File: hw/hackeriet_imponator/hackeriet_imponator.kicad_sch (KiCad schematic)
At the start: 19 parts, among them J1 USB4085-GF-A, J2 UPDI Programming, J3 External Battery Connector, J4 Shitty Add On, J5 Unused pins, SW1 SW_SPDT, U1 ATtiny804-SS, U2 MCP2221AxSL

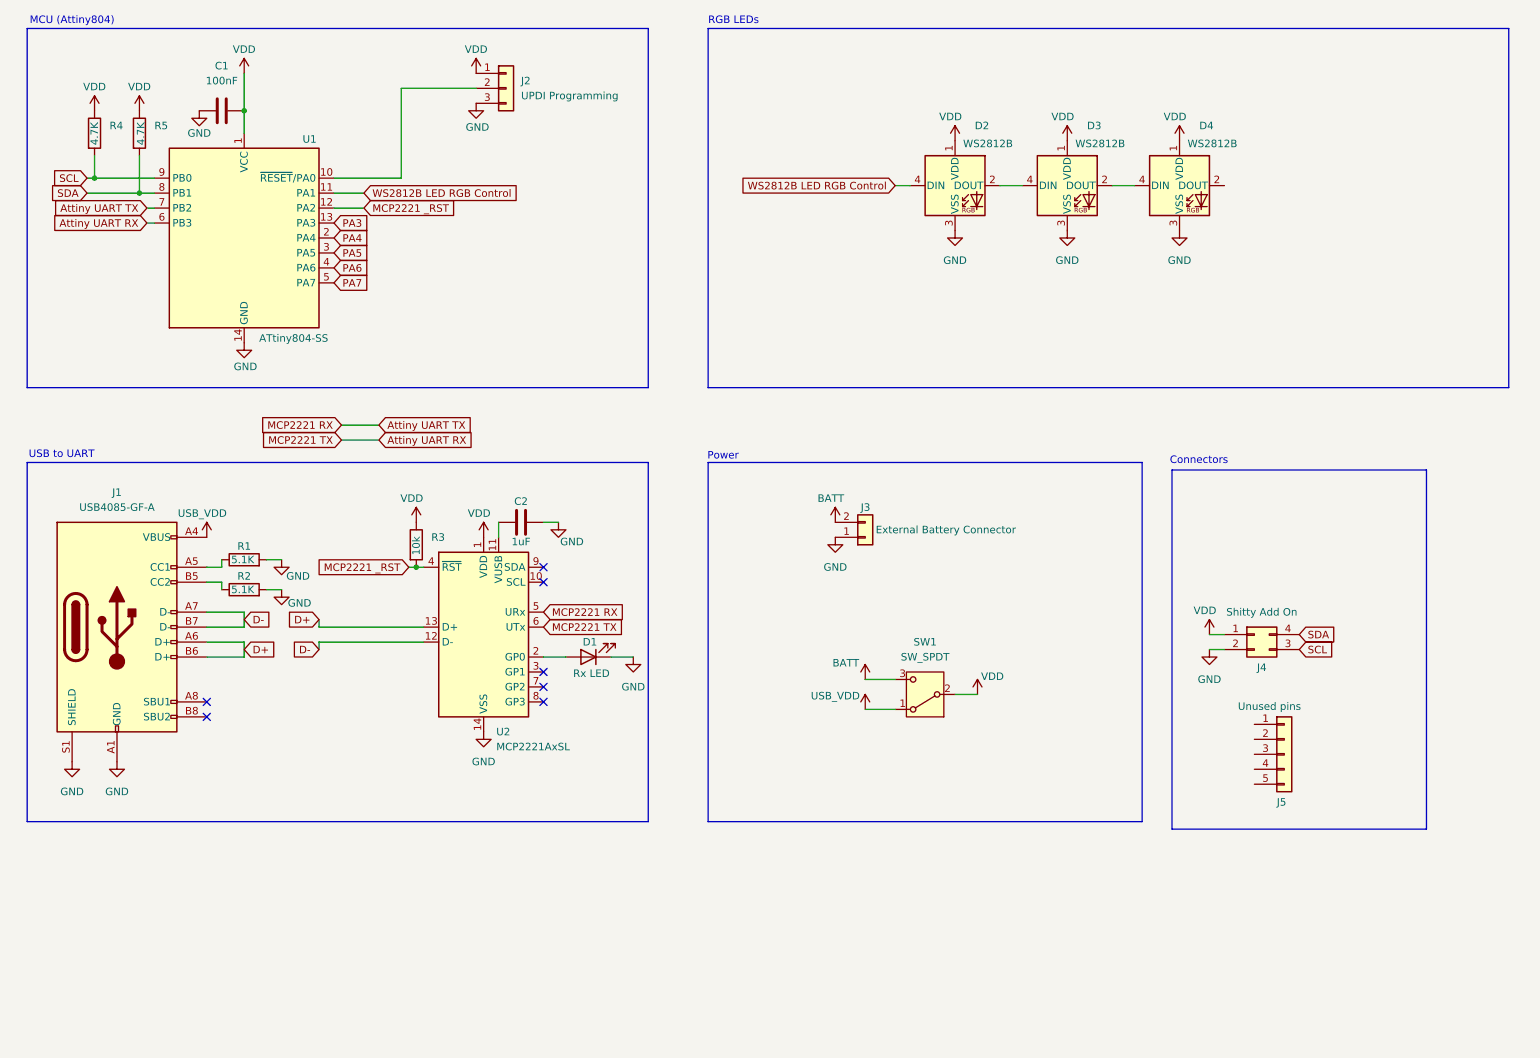
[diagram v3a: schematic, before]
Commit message: Fine-tuned silkscreen logo and LED spacing.
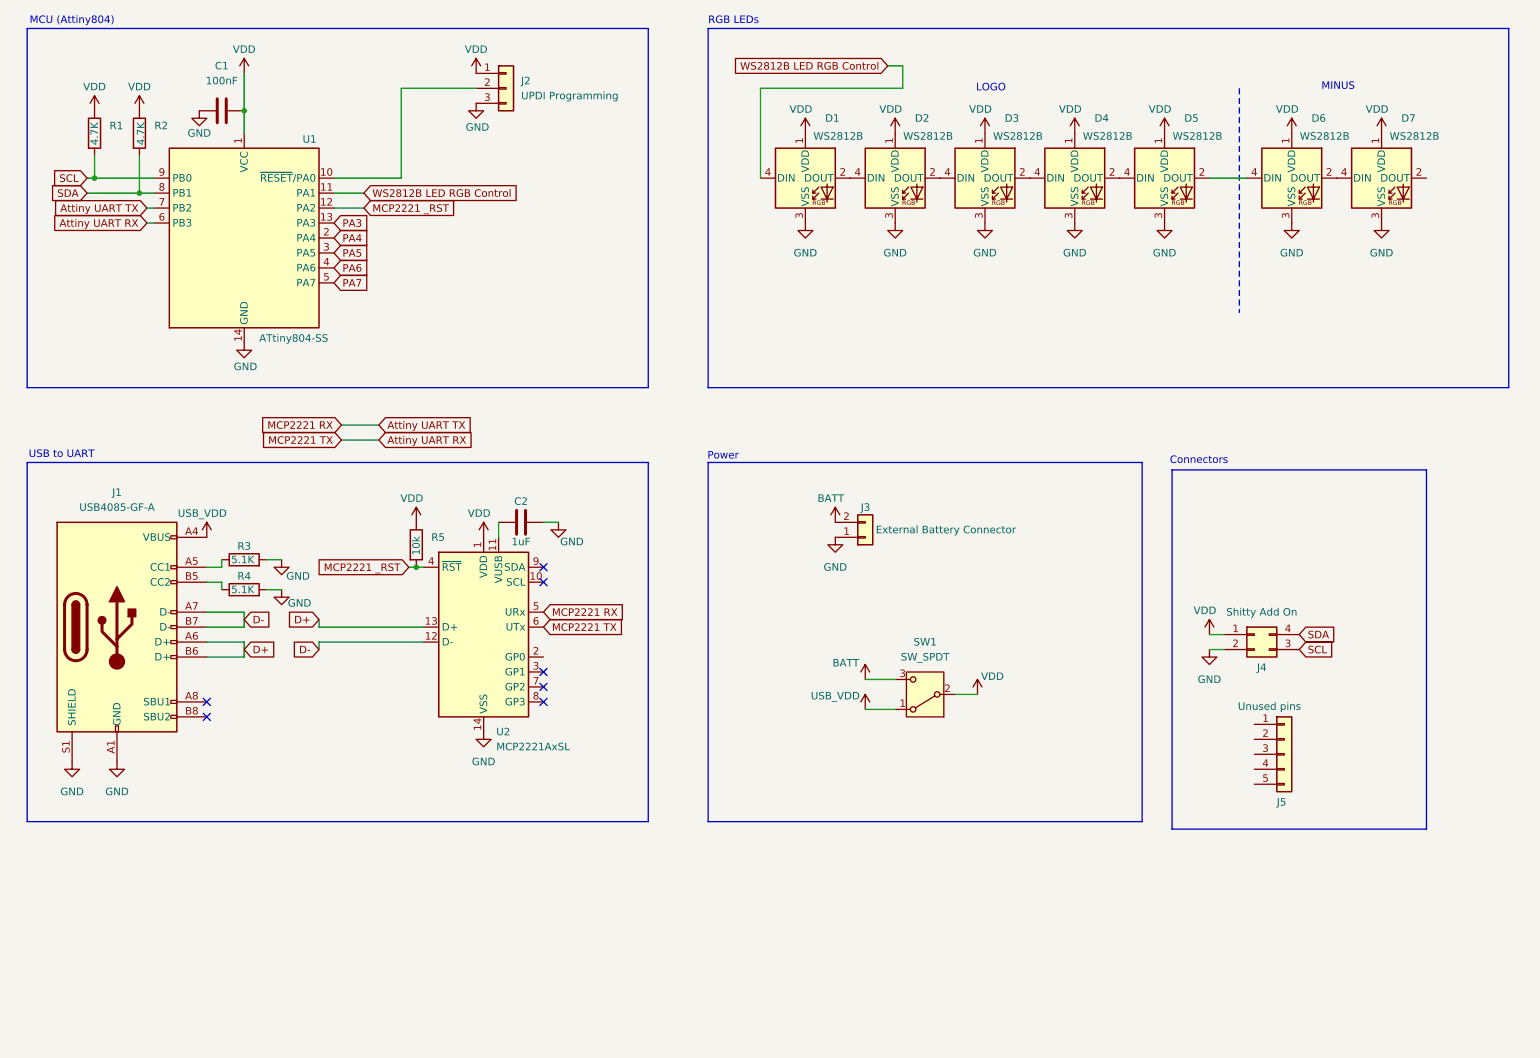
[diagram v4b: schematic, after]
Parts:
- removed D1: Rx LED, LED_SMD:LED_0603_1608Metric_Pad1.05x0.95mm_HandSolder, symbol Device:LED
- added D4, D5, D6, D7: WS2812B, imponator_footprint_lib:LED_WS2812B-4020, symbol LED:WS2812B
- renumbered D2 to D1, D4 to D2, R4 to R1, R5 to R2, R1 to R3, R2 to R4, R3 to R5
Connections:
- net GND: now also D4.3 (VSS), D5.3 (VSS), D6.3 (VSS), D7.3 (VSS)
- net VDD: now also D4.1 (VDD), D5.1 (VDD), D6.1 (VDD), D7.1 (VDD)
- net at D1.2 (DOUT): now also D2.4 (DIN); no longer D3.4 (DIN)
- net at D2.2 (DOUT): now also D3.4 (DIN)
- net at D3.2 (DOUT): now also D4.4 (DIN); no longer D2.4 (DIN)
- new net: D6.2 (DOUT), D7.4 (DIN)
- new net: D5.2 (DOUT), D6.4 (DIN)
- new net: D4.2 (DOUT), D5.4 (DIN)
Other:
- note added: "LOGO"
- note added: "MINUS"
- moved on the sheet: D1, D2

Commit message: Added accelerometer to schematic. Also crossed off some TODOs that were already done.
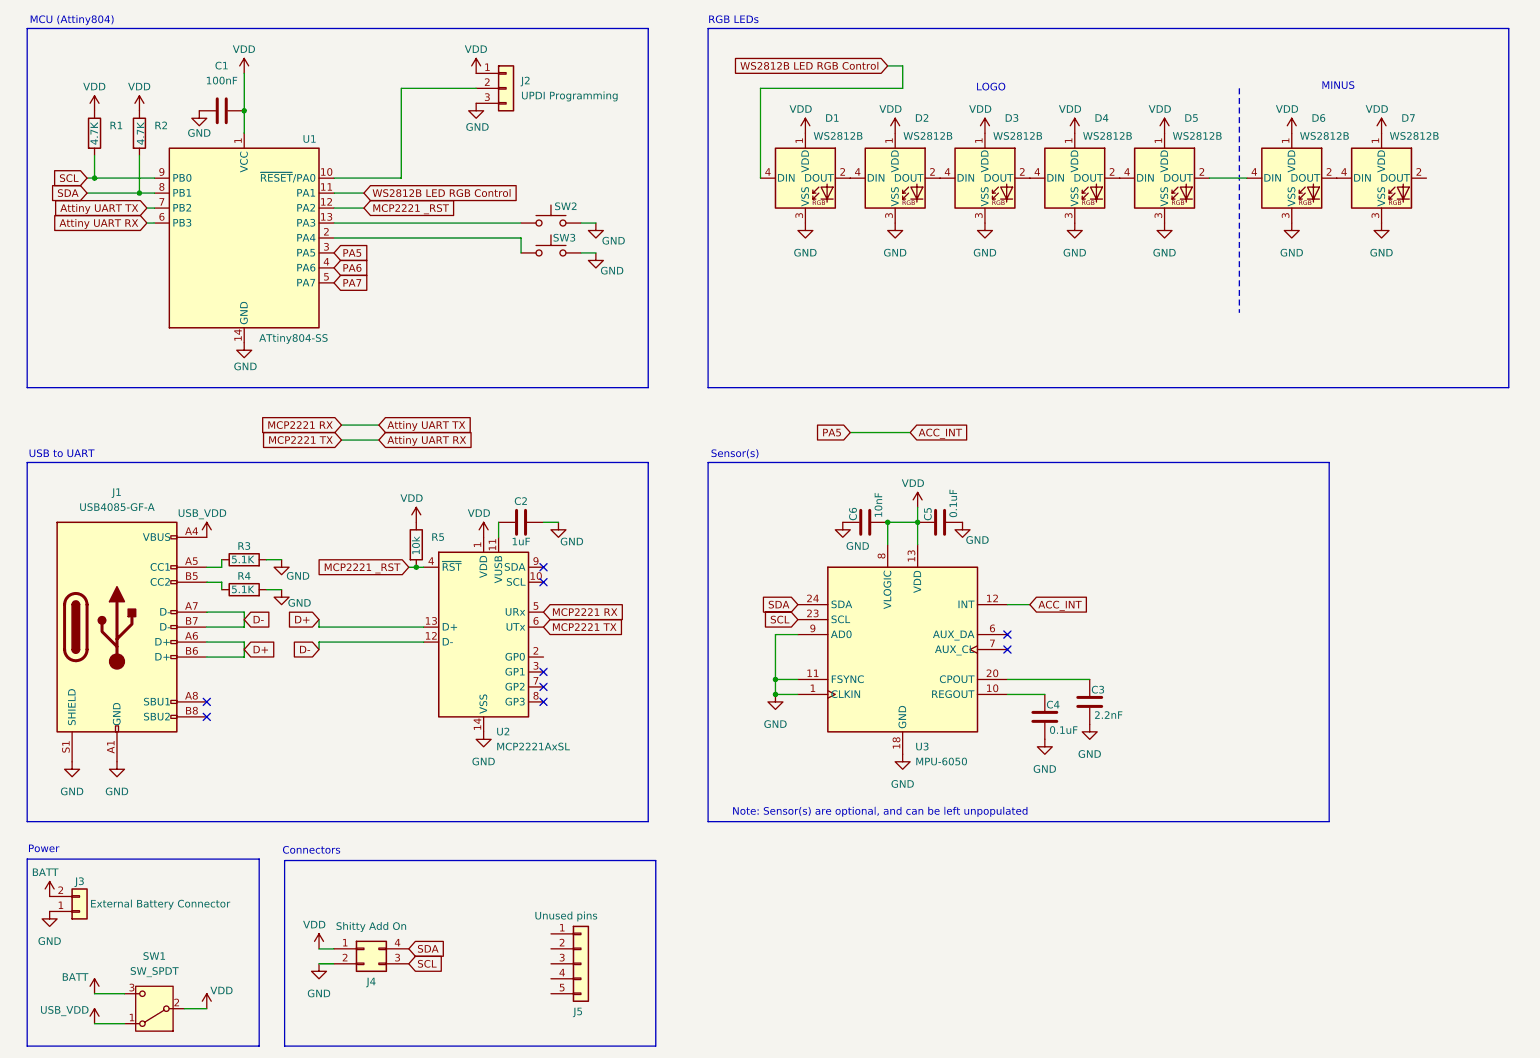
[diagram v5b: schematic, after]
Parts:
- added C3: 2.2nF, symbol Device:C
- added C4, C5: 0.1uF, symbol Device:C
- added C6: 10nF, symbol Device:C
- added SW2, SW3: User configurable, symbol Switch:SW_Push
- added U3: MPU-6050, Sensor_Motion:InvenSense_QFN-24_4x4mm_P0.5mm, symbol Sensor_Motion:MPU-6050
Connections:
- net GND: now also C3.1, C4.1, C5.1, C6.2, SW2.2, SW3.2, U3.1 (CLKIN), U3.11 (FSYNC), U3.18 (GND), U3.9 (AD0)
- net SCL: now also U3.23 (SCL)
- net SDA: now also U3.24 (SDA)
- net VDD: now also C5.2, C6.1, U3.13 (VDD), U3.8 (VLOGIC)
- net PA3: no longer names the net of U1.13 (PA3)
- net PA3: now also SW2.1
- net PA4: no longer names the net of U1.2 (PA4)
- net PA4: now also SW3.1
- net PA5 renamed ACC_INT
- net ACC_INT: now also U3.12 (INT)
- new net: C4.2, U3.10 (REGOUT)
- new net: C3.2, U3.20 (CPOUT)
- no-connect marks 7 -> 9
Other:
- note added: "Note: Sensor(s) are optional, and can be left unpopulated"
- note added: "Sensor(s)"
- moved on the sheet: J3, J4, J5, SW1

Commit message: Added LDO for accelerometer
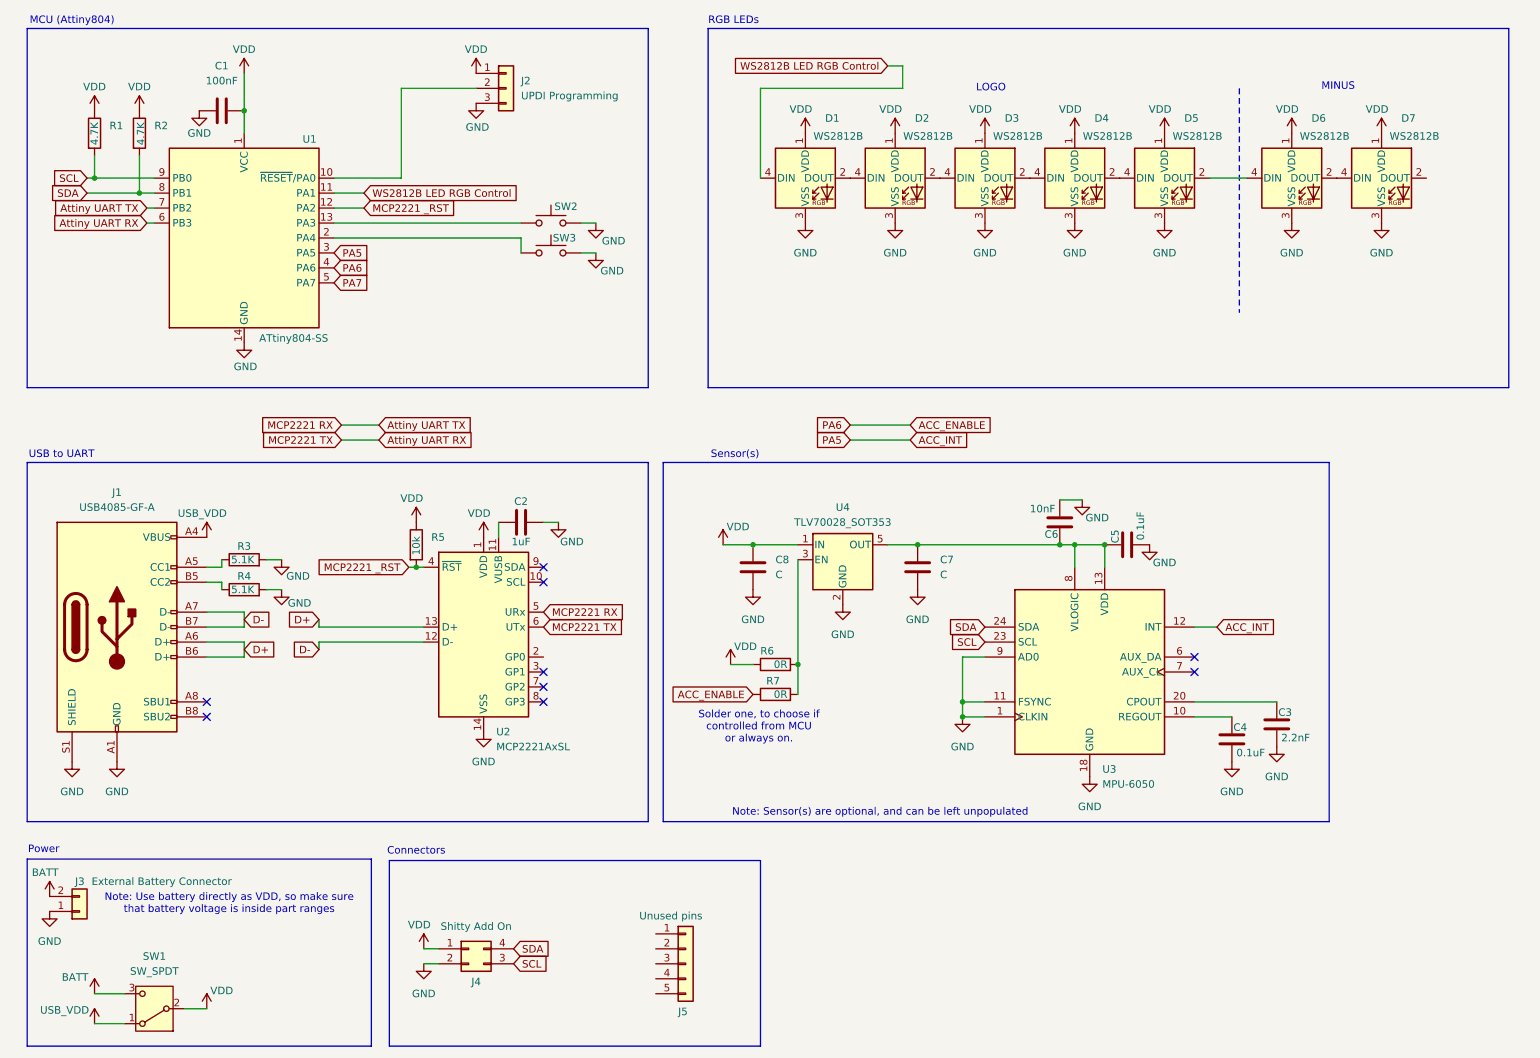
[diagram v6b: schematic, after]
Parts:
- added C7, C8: C, symbol Device:C
- added R6, R7: 0R, Resistor_SMD:R_0603_1608Metric_Pad0.98x0.95mm_HandSolder, symbol Device:R
- added U4: TLV70028_SOT353, Package_TO_SOT_SMD:SOT-353_SC-70-5, symbol Regulator_Linear:TLV70028_SOT353
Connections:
- net GND: now also C6.1, C7.2, C8.2, U4.2 (GND); no longer C6.2
- net VDD: now also C8.1, R6.1, U4.1 (IN); no longer C5.2, C6.1, U3.13 (VDD), U3.8 (VLOGIC)
- net PA6 renamed ACC_ENABLE
- net ACC_ENABLE: now also R7.1
- new net: C5.2, C6.2, C7.1, U3.13 (VDD), U3.8 (VLOGIC), U4.5 (OUT)
- new net: R6.2, R7.2, U4.3 (EN)
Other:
- note added: "Note: Use battery directly as VDD, so make sure that battery voltage is inside part ranges"
- note added: "Solder one, to choose if controlled from MCU or always on."
- moved on the sheet: C3, C4, C5, C6, J4, J5, U3

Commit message: Fixed LED pinout. Added PCB button. Distributed headers along side.
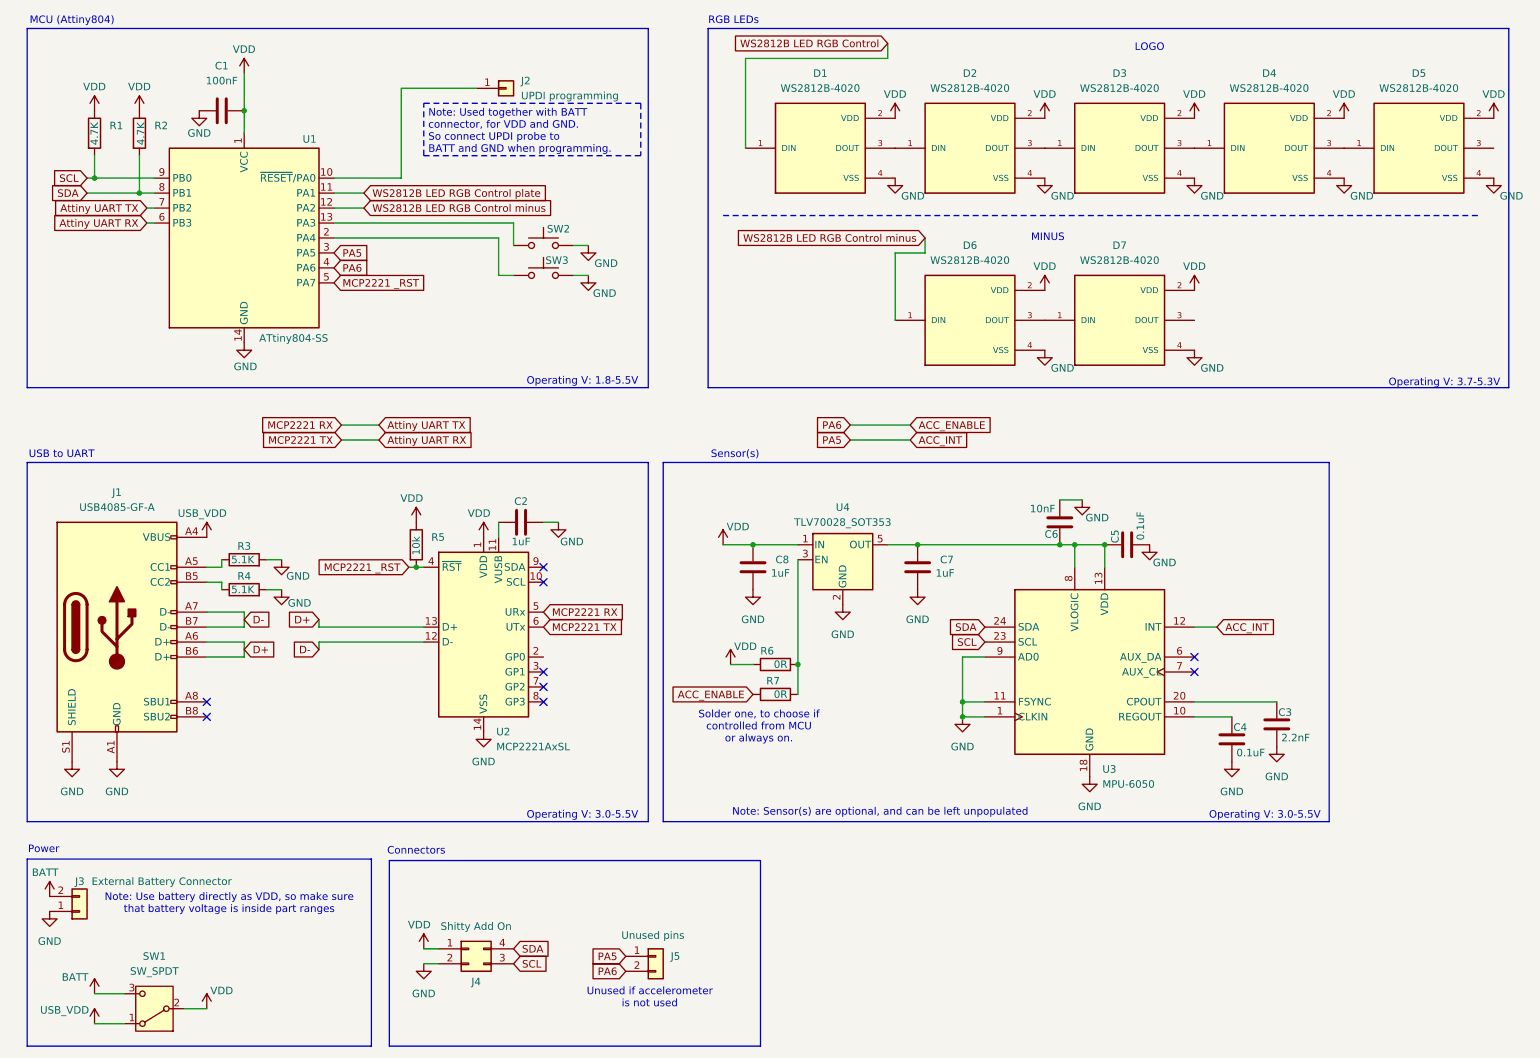
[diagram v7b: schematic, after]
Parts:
- removed D1, D2, D3, D4, D5, D6, D7: WS2812B, imponator_footprint_lib:LED_WS2812B-4020, symbol LED:WS2812B
- removed J2: UPDI Programming, Connector_PinHeader_2.54mm:PinHeader_1x03_P2.54mm_Horizontal, symbol Connector_Generic:Conn_01x03
- removed J5: Unused pins, Connector_PinSocket_2.54mm:PinSocket_1x05_P2.54mm_Vertical_SMD_Pin1Left, symbol Connector_Generic:Conn_01x05
- added D1, D2, D3, D4, D5, D6, D7: WS2812B-4020, WS2812B-4020:LED_WS2812B-4020, symbol WS2812B-4020:WS2812B-4020
- added J2: UPDI programming, Connector_Wire:SolderWirePad_1x01_SMD_2x4mm, symbol Connector_Generic:Conn_01x01
- added J5: Unused pins, Connector_PinSocket_2.54mm:PinSocket_1x02_P2.54mm_Vertical_SMD_Pin1Right, symbol Connector_Generic:Conn_01x02
- C3, C4, C5, C6: footprint (none) -> Capacitor_SMD:C_0603_1608Metric_Pad1.08x0.95mm_HandSolder
- C7, C8: value C -> 1uF; footprint (none) -> Capacitor_SMD:C_0603_1608Metric_Pad1.08x0.95mm_HandSolder
- SW2, SW3: footprint (none) -> Button_Switch_SMD:SW_SPST_EVQP7C
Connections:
- net PA7 is gone; now on net MCP2221 _RST: U1.5 (PA7)
- net ACC_ENABLE: now also J5.2 (Pin_2)
- net ACC_INT: now also J5.1 (Pin_1)
- net GND: now also D1.4 (VSS), D2.4 (VSS), D3.4 (VSS), D4.4 (VSS), D5.4 (VSS), D6.4 (VSS), D7.4 (VSS)
- net MCP2221 _RST: no longer U1.12 (PA2)
- net VDD: now also D1.2 (VDD), D2.2 (VDD), D3.2 (VDD), D4.2 (VDD), D5.2 (VDD), D6.2 (VDD), D7.2 (VDD)
- net WS2812B LED RGB Control: now also D1.1 (DIN); no longer U1.11 (PA1)
- net at U1.10 (~{RESET}/PA0): now also J2.1 (Pin_1)
- new net: D2.3 (DOUT), D3.1 (DIN)
- new net: D3.3 (DOUT), D4.1 (DIN)
- new net: D4.3 (DOUT), D5.1 (DIN)
- new net: D6.3 (DOUT), D7.1 (DIN)
- new net: D1.3 (DOUT), D2.1 (DIN)
- new net WS2812B LED RGB Control minus: D6.1 (DIN), U1.12 (PA2)
- new net WS2812B LED RGB Control plate: U1.11 (PA1)
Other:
- note added: "Note: Used together with BATT connector, for VDD and GND. So connect UPDI probe to BATT and GND when programming."
- note added: "Operating V: 1.8-5.5V"
- note added: "Operating V: 3.0-5.5V"
- note added: "Operating V: 3.7-5.3V"
- note added: "Unused if accelerometer is not used"
- moved on the sheet: SW2, SW3
